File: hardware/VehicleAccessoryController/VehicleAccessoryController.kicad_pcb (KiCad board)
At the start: 2 copper layers, 140.6 x 76 mm, 1 part, among them U1 REM30-2405SW

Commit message: schematic updates, begin layout
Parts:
- removed U1: REM30-2405SW, VehicleAccessoryController:REM30-XXXXXW
- added C801: 10uF, VehicleAccessoryController:C_2917_D, F.Cu at (47.1, 65.3)
- added C802: 1uF, VehicleAccessoryController:C_0603, F.Cu at (131.8, 47.2)
- added C803: 0.1uF, VehicleAccessoryController:C_0603, F.Cu at (138.4, 62.2)
- added C804: 0.1uF, VehicleAccessoryController:C_0603, F.Cu at (34.7, 93.9)
- added C805: 0.1uF, VehicleAccessoryController:C_0603, F.Cu at (69.0, 140.2)
- added C806: 4.7uF, VehicleAccessoryController:C_0603, F.Cu at (158.6, 151.4)
- added C807: 0.1uF, VehicleAccessoryController:C_0603, F.Cu at (158.6, 147.1)
- added C808: 4.7uF, VehicleAccessoryController:C_0603, F.Cu at (158.5, 155.1)
- added C809: 0.1uF, VehicleAccessoryController:C_0603, F.Cu at (158.4, 142.8)
- added C810: 0.1nF, VehicleAccessoryController:C_0603, F.Cu at (124.6, 164.5)
- added C811: 0.1uF, VehicleAccessoryController:C_0603, F.Cu at (149.0, 157.2)
- added C812: 0.1uF, VehicleAccessoryController:C_0603, F.Cu at (193.1, 146.9)
- added C813: 0.1uF, VehicleAccessoryController:C_0603, F.Cu at (204.3, 146.3)
- added D601: LED_ALT, VehicleAccessoryController:LED_0603, F.Cu at (199.1, 27.2)
- added D602: LED_ALT, VehicleAccessoryController:LED_0603, F.Cu at (199.0, 31.9)
- added D603: LED_ALT, VehicleAccessoryController:LED_0603, F.Cu at (199.1, 36.7)
- added D604: LED_ALT, VehicleAccessoryController:LED_0603, F.Cu at (199.1, 41.2)
- added D605: SP0503BAHT, Package_TO_SOT_SMD:SOT-143, F.Cu at (101.8, 156.3)
- added F401: Fuse, VehicleAccessoryController:Littelfuse_01530007, F.Cu at (41.5, 51.4)
- added J501: Input, VehicleAccessoryController:Keystone_8719, F.Cu at (20.6, 45.0)
- added J502: Front Conn, VehicleAccessoryController:TE_1776275-3, F.Cu at (237.5, 73.4)
- added J503: Rear Conn, VehicleAccessoryController:TE_1776275-3, F.Cu at (236.8, 89.9)
- added J504: Left Conn, VehicleAccessoryController:TE_1776275-3, F.Cu at (235.9, 109.7)
- added J505: Right Conn, VehicleAccessoryController:TE_1776275-3, F.Cu at (237.6, 132.0)
- added J506: USB_B_Mini, VehicleAccessoryController:AFCI_10033526_USB-mini, F.Cu at (113.3, 156.5)
- added P601: TC2030-MCP, Tag-Connect:TC2030_SMALL, F.Cu at (152.7, 55.0)
- added Q201: BSS138, Package_TO_SOT_SMD:SOT-23, F.Cu at (227.4, 73.2)
- added Q202: BSS138, Package_TO_SOT_SMD:SOT-23, F.Cu at (228.2, 89.5)
- added Q203: BSS138, Package_TO_SOT_SMD:SOT-23, F.Cu at (226.1, 110.2)
- added Q204: BSS138, Package_TO_SOT_SMD:SOT-23, F.Cu at (227.3, 132.0)
- added R701: 48k7, VehicleAccessoryController:R_0603, F.Cu at (75.9, 61.4)
- added R702: 10K, VehicleAccessoryController:R_0603, F.Cu at (139.8, 45.6)
- added R703: 2M43, VehicleAccessoryController:R_0603, F.Cu at (39.4, 97.6)
- added R704: 84k5, VehicleAccessoryController:R_0603, F.Cu at (39.8, 94.1)
- added R705: 49k9, VehicleAccessoryController:R_0603, F.Cu at (64.4, 62.3)
- added R706: 430R, VehicleAccessoryController:R_0603, F.Cu at (191.9, 27.2)
- added R707: 430R, VehicleAccessoryController:R_0603, F.Cu at (191.8, 31.9)
- added R708: 1k, VehicleAccessoryController:R_0603, F.Cu at (218.9, 71.0)
- added R709: 1k, VehicleAccessoryController:R_0603, F.Cu at (220.4, 91.3)
- added R710: 1k, VehicleAccessoryController:R_0603, F.Cu at (211.8, 111.2)
- added R711: 1k, VehicleAccessoryController:R_0603, F.Cu at (219.4, 130.4)
- added R712: 1M, VehicleAccessoryController:R_0603, F.Cu at (211.5, 75.2)
- added R713: 1M, VehicleAccessoryController:R_0603, F.Cu at (220.7, 88.0)
- added R714: 1M, VehicleAccessoryController:R_0603, F.Cu at (218.9, 111.3)
- added R715: 1M, VehicleAccessoryController:R_0603, F.Cu at (219.4, 133.9)
- added R716: 22k1, VehicleAccessoryController:R_0603, F.Cu at (218.8, 74.4)
- added R717: 22k1, VehicleAccessoryController:R_0603, F.Cu at (212.4, 88.1)
- added R718: 22k1, VehicleAccessoryController:R_0603, F.Cu at (211.5, 107.5)
- added R719: 22k1, VehicleAccessoryController:R_0603, F.Cu at (212.0, 130.3)
- added R720: 30k9, VehicleAccessoryController:R_0603, F.Cu at (211.6, 71.0)
- added R721: 30k9, VehicleAccessoryController:R_0603, F.Cu at (212.4, 91.8)
- added R722: 30k9, VehicleAccessoryController:R_0603, F.Cu at (219.5, 107.6)
- added R723: 30k9, VehicleAccessoryController:R_0603, F.Cu at (211.8, 134.1)
- added R724: 1k, VehicleAccessoryController:R_0603, F.Cu at (61.3, 140.8)
- added R725: 160R, VehicleAccessoryController:R_0603, F.Cu at (77.4, 147.3)
- added R726: 1k, VehicleAccessoryController:R_0603, F.Cu at (76.9, 141.4)
- added R727: 1M, VehicleAccessoryController:R_0603, F.Cu at (124.5, 161.0)
- added R728: 1k, VehicleAccessoryController:R_0603, F.Cu at (148.9, 143.0)
- added R729: 90R, VehicleAccessoryController:R_0603, F.Cu at (191.4, 36.8)
- added R730: 90R, VehicleAccessoryController:R_0603, F.Cu at (190.6, 41.4)
- added R731: 22.1k, VehicleAccessoryController:R_0603, F.Cu at (140.7, 136.9)
- added R732: 47.5k, VehicleAccessoryController:R_0603, F.Cu at (140.9, 140.2)
- added SW301: ON/OFF, VehicleAccessoryController:C&K_ET_Series_Switch, F.Cu at (38.7, 126.5)
- added U101: RECOM_REMX0-W, VehicleAccessoryController:REM20-XXXXXW, F.Cu at (76.8, 41.2)
- added U102: ATMEGA328P-M(32QFN_MLF), VehicleAccessoryController:ATMEGA328P-MU_VQFN_MLF32, F.Cu at (138.4, 54.2)
- added U103: TPS3710, VehicleAccessoryController:TI DSE (S-PWSON-N6), F.Cu at (34.4, 100.1)
- added U104: SI8710CC-B-IS, VehicleAccessoryController:SOIC-8_NB, F.Cu at (68.7, 147.9)
- added U105: CP2102N-A02-GQFN24, Package_DFN_QFN:QFN-24-1EP_4x4mm_P0.5mm_EP2.6x2.6mm, F.Cu at (149.2, 150.8)
- added U106: Si8621BB-B-IS, Package_SO:SOIC-8_3.9x4.9mm_P1.27mm, F.Cu at (199.3, 151.7)
- added Y901: 16MHz, VehicleAccessoryController:CSTNE_Resonator, F.Cu at (131.1, 55.1)
- added fid1: FID, VehicleAccessoryController:Fiducial, F.Cu at (36.7, 25.0)
- added fid2: FID, VehicleAccessoryController:Fiducial, F.Cu at (46.9, 163.9)
- added fid3: FID, VehicleAccessoryController:Fiducial, F.Cu at (204.0, 165.3)
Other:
- board size 140.6 x 76 mm -> 242.3 x 150.3 mm

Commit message: test board PDFs, label updates, merge duplicates on BOMs
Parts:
- R731: value 22.1k -> 22k1
- R732: value 47.5k -> 47k5
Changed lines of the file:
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@@
   (title_block
     (title "Vehicle Accessory Controller")
-    (date 2019-11-20)
+    (date 2019-11-22)
     (rev 0.1)
     (company Noctivore)
@@
       (effects (font (size 1 1) (thickness 0.15)))
     )
-    (fp_text value 22.1k (at 3.5 0) (layer F.Fab)
+    (fp_text value 22k1 (at 3.5 0) (layer F.Fab)
       (effects (font (size 1 1) (thickness 0.15)))
     )
@@
       (effects (font (size 1 1) (thickness 0.15)))
     )
-    (fp_text value 47.5k (at 3.5 0) (layer F.Fab)
-      (effects (font (size 1 1) (thickness 0.15)))
-    )
+    (fp_text value 47k5 (at 3.5 0) (layer F.Fab)
+      (effects (font (size 1 1) (thickness 0.15)))
+    )

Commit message: shcematic updates
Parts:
- added C814: 1uF, VehicleAccessoryController:C_0603, F.Cu at (116.3, 61.3)
- added C815: 1uF, VehicleAccessoryController:C_0603, F.Cu at (121.9, 67.2)
- added REF**: FAB_NOTES, VehicleAccessoryController:FAB_NOTES, F.Cu at (12.0, 12.0)
- added U107: NCV551SN50T1G, Package_TO_SOT_SMD:SOT-23-5, F.Cu at (117.2, 67.3)
- U106: value Si8621BB-B-IS -> Si8631EC-B-IS1; footprint Package_SO:SOIC-8_3.9x4.9mm_P1.27mm -> Package_SO:SOIC-16_3.9x9.9mm_P1.27mm
- moved C811 59.6 mm to (208.4, 152.0), turned to 180 degrees
- moved fid1 48.9 mm to (35.0, 73.9)
- moved U101 15.8 mm to (76.9, 57.0)
- moved F401 15.0 mm to (40.8, 66.4)
- moved R701 15.0 mm to (75.2, 76.4)
- moved C801 15.0 mm to (46.4, 80.3)
- moved J501 15.0 mm to (19.9, 60.0)
- moved R705 15.0 mm to (63.7, 77.3)
- moved R703 4.60 mm to (39.3, 102.2)
- moved U103 4.60 mm to (34.3, 104.7)
- moved R704 4.60 mm to (39.7, 98.7)
- moved C804 4.60 mm to (34.6, 98.5)
- moved U106 2.90 mm to (199.3, 154.6)
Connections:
- net /328P_RESET renamed /328P_RST
- net /328P_SS renamed Net-(U102-Pad14)
- U105 pad 23: Net-(C811-Pad2) -> /CP2102N_RST
- U106 pad 2: /CP2102N_TXD -> GNDD
- U106 pad 3: /CP2102N_RXD -> /CP2102N_RST
- U106 pad 4: GNDD -> /CP2102N_TXD
- U106 pad 5: GND -> /CP2102N_RXD
- U106 pad 6: /328P_TXD -> Net-(U106-Pad6)
- U106 pad 7: /328P_RXD -> VDD
- U106 pad 8: +5VD -> GNDD
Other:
- board size 242.3 x 150.3 mm -> 242.3 x 146.4 mm

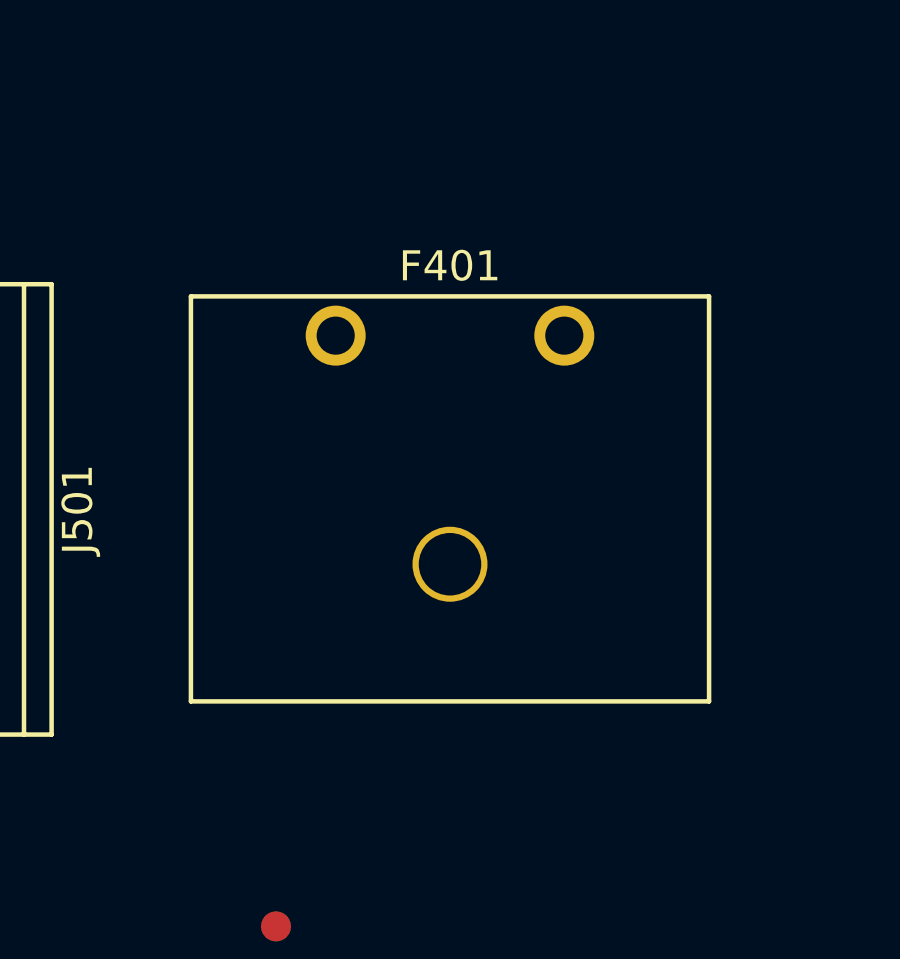
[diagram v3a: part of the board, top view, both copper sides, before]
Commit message: correct fuse holder, ACC pull-up, BOM Accessories, create firmware dir
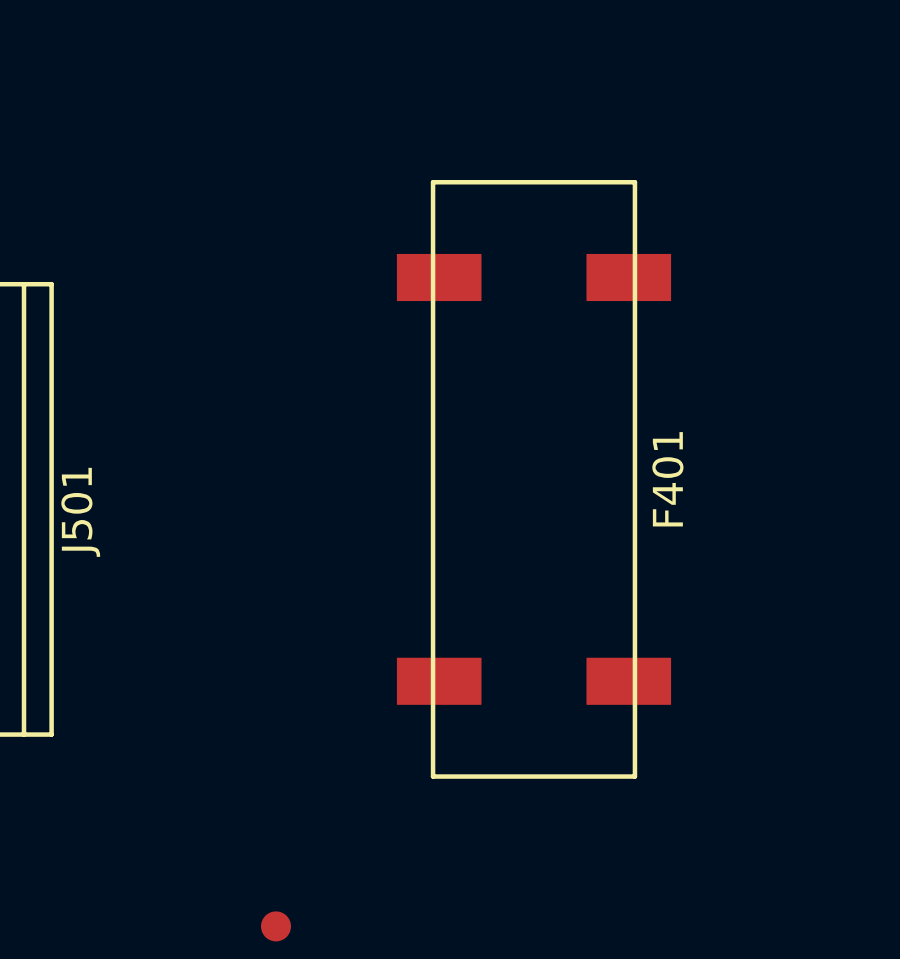
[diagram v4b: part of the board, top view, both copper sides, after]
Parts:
- F401: footprint VehicleAccessoryController:Littelfuse_01530007 -> VehicleAccessoryController:Keystone_3587
- moved F401 7.91 mm to (43.6, 59.0), turned to 270 degrees
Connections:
- R725 pad 2: Net-(R725-Pad2) -> /ACC_OUT
- R726 pad 2: /ACC -> /ACC_OUT
- U104 pad 6: Net-(R725-Pad2) -> /ACC_OUT
